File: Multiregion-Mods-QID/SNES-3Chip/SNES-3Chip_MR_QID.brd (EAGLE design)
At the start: 88.9 x 37.1 mm, 27 parts, among them IC1 74HC27D, IC2 74HC30D

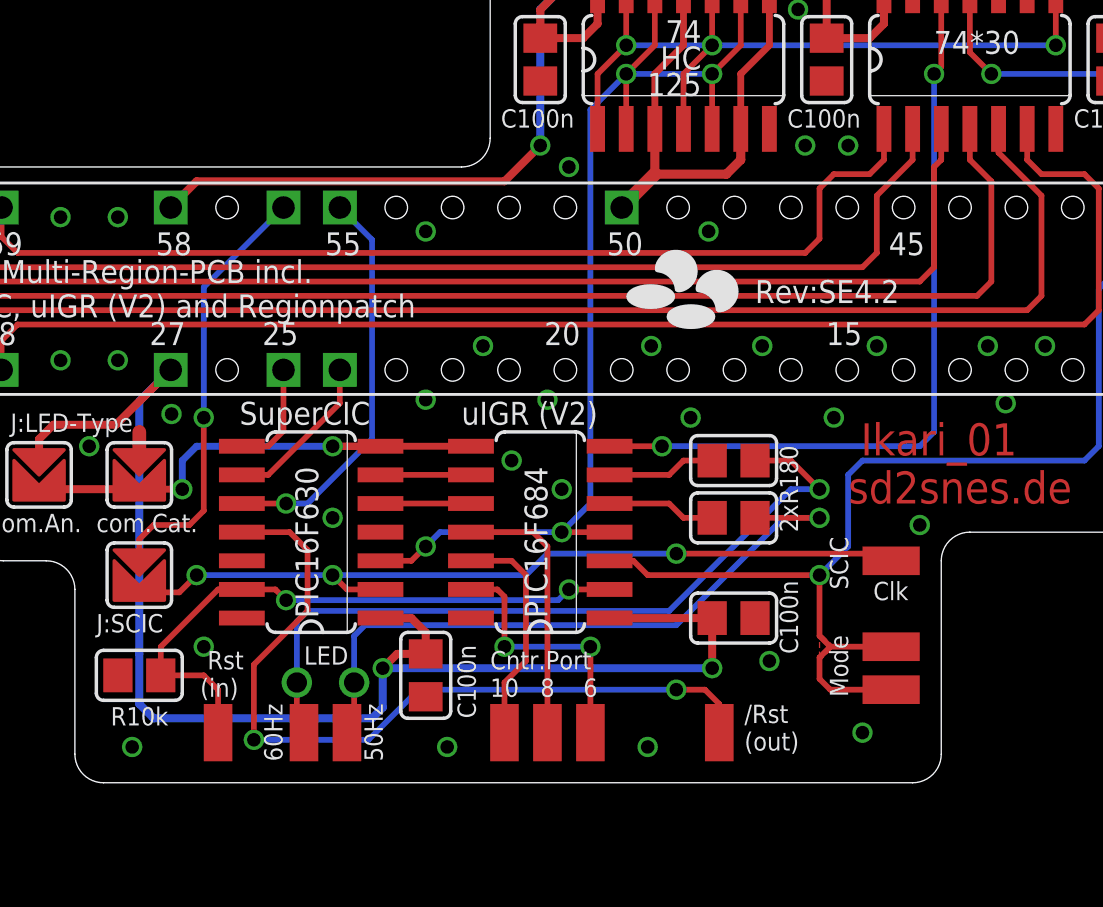
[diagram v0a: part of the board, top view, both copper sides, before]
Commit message: Minor Updates: - Dual design for crystals (SNES-1Chip_MR_QID only); SMD and THT crystals are now supported (If THT crystals are used, SMD pads have to isolated, manually.) - minor tweaks of traces - EAGLE Version 7.5.0
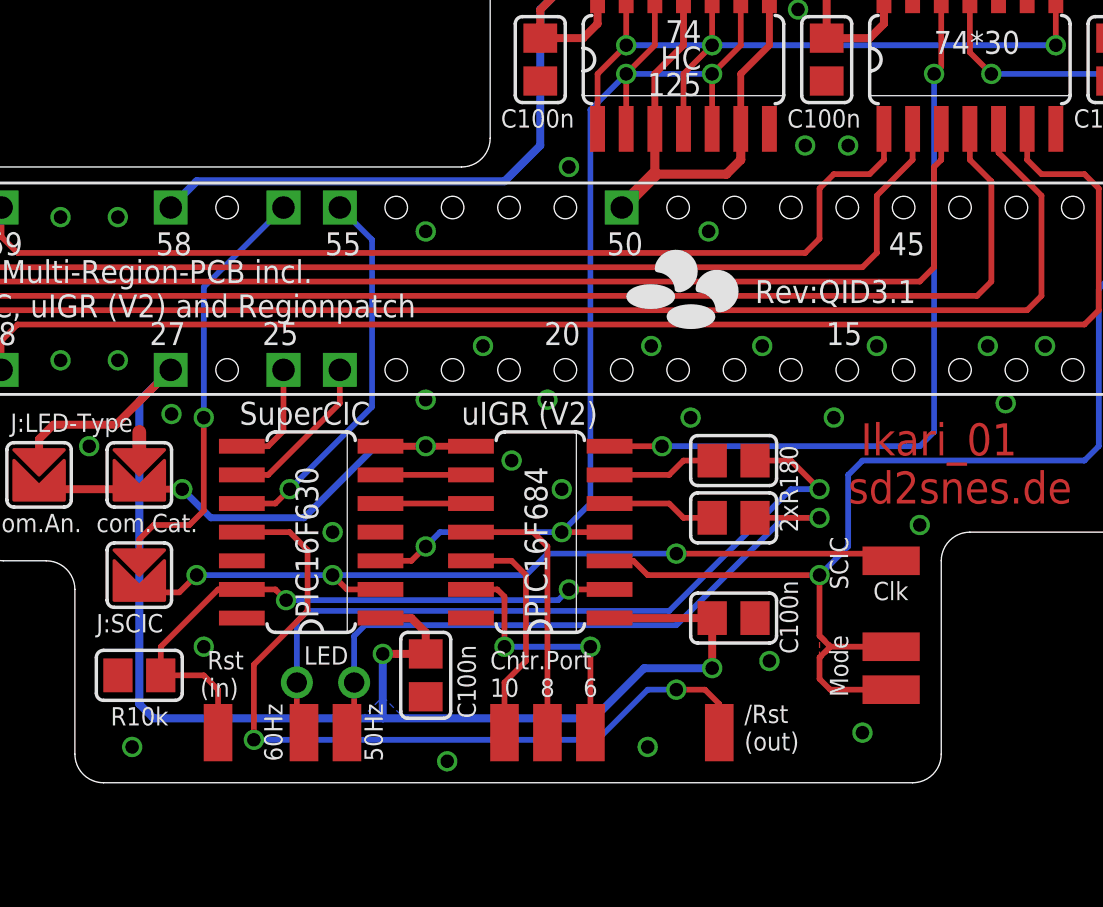
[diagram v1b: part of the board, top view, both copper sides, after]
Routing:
- net VCC: track 63.2 -> 64.8 mm
- net N$48: track 17.8 -> 17.0 mm
- net VCC_2: vias 4 -> 3
- added copper zone on layer 16, net VCC
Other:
- board text added: "Rev:QID3.1"
- board text removed: "Rev:SE4.2"
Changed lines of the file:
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@@
 <?xml version="1.0" encoding="utf-8"?>
 <!DOCTYPE eagle SYSTEM "eagle.dtd">
-<eagle version="7.4.0">
+<eagle version="7.5.0">
 <drawing>
 <settings>
@@
 <wire x1="52.3875" y1="15.875" x2="52.3875" y2="7.3025" width="0" layer="20"/>
 <wire x1="52.3875" y1="7.3025" x2="51.1175" y2="6.0325" width="0" layer="20" curve="-90"/>
-<text x="44.1325" y="27.305" size="1.016" layer="25" font="vector" ratio="12">Rev:SE4.2</text>
+<text x="44.1325" y="27.305" size="1.016" layer="25" font="vector" ratio="12">Rev:QID3.1</text>
 <polygon width="0.1" layer="21">
 <vertex x="40.534165625" y="27.590709375"/>
@@
 <signal name="GND">
 <contactref element="C1" pad="2"/>
-<via x="25.4" y="17.78" extent="1-16" drill="0.6"/>
+<via x="25.4" y="17.145" extent="1-16" drill="0.6"/>
 <via x="84.455" y="27.94" extent="1-16" drill="0.6"/>
 <via x="88.265" y="27.94" extent="1-16" drill="0.6"/>
@@
 <via x="44.45" y="25.4" extent="1-16" drill="0.6"/>
 <via x="19.685" y="12.065" extent="1-16" drill="0.6"/>
-<via x="30.48" y="7.62" extent="1-16" drill="0.6"/>
+<via x="30.48" y="6.985" extent="1-16" drill="0.6"/>
 <via x="33.655" y="41.275" extent="1-16" drill="0.6"/>
 <via x="39.52875" y="25.4" extent="1-16" drill="0.6"/>
@@
 <contactref element="C2" pad="1"/>
 <wire x1="37.6809" y1="13.335" x2="42.23" y2="13.335" width="0.3556" layer="1"/>
-<via x="27.6225" y="11.1125" extent="1-16" drill="0.6"/>
+<via x="27.6225" y="11.7475" extent="1-16" drill="0.6"/>
 <wire x1="27.5209" y1="13.335" x2="28.8925" y2="13.335" width="0.3556" layer="1"/>
 <wire x1="28.8925" y1="13.335" x2="29.5275" y2="12.7" width="0.3556" layer="1"/>
 <wire x1="29.5275" y1="12.7" x2="29.5275" y2="11.745" width="0.3556" layer="1"/>
-<wire x1="27.6225" y1="11.1125" x2="28.26" y2="11.7475" width="0.3556" layer="1"/>
 <wire x1="28.26" y1="11.7475" x2="29.5275" y2="11.745" width="0.3556" layer="1"/>
 <via x="42.23" y="11.115" extent="1-16" drill="0.6"/>
 <contactref element="U$6" pad="27"/>
 <wire x1="12.3825" y1="20.32" x2="12.3825" y2="21.2725" width="0.3556" layer="1"/>
-<wire x1="16.8275" y1="11.7475" x2="16.8275" y2="22.9475" width="0.3556" layer="16"/>
+<wire x1="16.8275" y1="9.525" x2="16.8275" y2="22.9475" width="0.3556" layer="16"/>
 <wire x1="16.8275" y1="22.9475" x2="18.22" y2="24.34" width="0.3556" layer="16"/>
 <wire x1="12.3825" y1="21.2725" x2="13.0175" y2="21.9075" width="0.3556" layer="1"/>
@@
 <wire x1="15.7875" y1="21.9075" x2="18.22" y2="24.34" width="0.3556" layer="1"/>
 <wire x1="42.23" y1="11.115" x2="42.23" y2="13.335" width="0.3556" layer="1"/>
-<wire x1="27.6225" y1="11.1125" x2="42.2275" y2="11.1125" width="0.3556" layer="16"/>
 <wire x1="42.2275" y1="11.1125" x2="42.23" y2="11.115" width="0.3048" layer="16"/>
-<wire x1="16.8275" y1="11.7475" x2="16.8275" y2="9.525" width="0.3556" layer="16"/>
 <wire x1="16.8275" y1="9.525" x2="17.4625" y2="8.89" width="0.3556" layer="16"/>
-<wire x1="17.4625" y1="8.89" x2="27.14625" y2="8.89" width="0.3556" layer="16"/>
-<wire x1="27.14625" y1="8.89" x2="27.6225" y2="9.36625" width="0.3556" layer="16"/>
-<wire x1="27.6225" y1="9.36625" x2="27.6225" y2="11.1125" width="0.3556" layer="16"/>
+<wire x1="17.4625" y1="8.89" x2="27.6225" y2="8.89" width="0.3556" layer="16"/>
+<wire x1="27.6225" y1="8.89" x2="36.98875" y2="8.89" width="0.3556" layer="16"/>
+<wire x1="42.2275" y1="11.1125" x2="39.21125" y2="11.1125" width="0.3556" layer="16"/>
+<wire x1="39.21125" y1="11.1125" x2="36.98875" y2="8.89" width="0.3556" layer="16"/>
+<wire x1="27.6225" y1="11.7475" x2="27.6225" y2="8.89" width="0.3556" layer="16"/>
+<wire x1="28.26" y1="11.7475" x2="27.6225" y2="11.7475" width="0.3556" layer="1"/>
+<polygon width="0.3556" layer="16">
+<vertex x="26.67" y="8.89"/>
+<vertex x="27.6225" y="9.8425"/>
+<vertex x="28.575" y="8.89"/>
+</polygon>
 </signal>
 <signal name="N$42">
@@
 <contactref element="IC2" pad="14"/>
 <contactref element="74HC(T)125" pad="14"/>
-<wire x1="18.22" y1="31.54" x2="18.22" y2="31.555" width="0.3048" layer="1"/>
-<wire x1="18.22" y1="31.555" x2="19.3675" y2="32.7025" width="0.3556" layer="1"/>
-<via x="34.6075" y="34.29" extent="1-16" drill="0.6"/>
 <wire x1="35.56" y1="41.275" x2="47.3075" y2="41.275" width="0.3556" layer="16"/>
 <via x="60.0075" y="41.275" extent="1-16" drill="0.6"/>
@@
 <wire x1="47.31" y1="39.0525" x2="47.3075" y2="39.0525" width="0.3048" layer="1"/>
 <wire x1="47.3075" y1="39.0525" x2="47.3075" y2="41.275" width="0.3556" layer="1"/>
-<wire x1="19.3675" y1="32.7025" x2="33.02" y2="32.7025" width="0.3556" layer="1"/>
-<wire x1="33.02" y1="32.7025" x2="34.6075" y2="34.29" width="0.3556" layer="1"/>
 <wire x1="35.56" y1="41.275" x2="34.6075" y2="40.3225" width="0.3556" layer="16"/>
 <wire x1="34.6075" y1="40.3225" x2="34.6075" y2="34.29" width="0.3556" layer="16"/>
+<wire x1="18.22" y1="31.555" x2="19.3675" y2="32.7025" width="0.3556" layer="16"/>
+<wire x1="19.3675" y1="32.7025" x2="33.02" y2="32.7025" width="0.3556" layer="16"/>
+<wire x1="33.02" y1="32.7025" x2="34.6075" y2="34.29" width="0.3556" layer="16"/>
+<wire x1="18.22" y1="31.555" x2="18.22" y2="31.54" width="0" layer="19" extent="16-16"/>
 </signal>
 <signal name="N$39">
@@
 <contactref element="U$2" pad="10"/>
 <contactref element="U$6" pad="55"/>
-<wire x1="27.14625" y1="21.2725" x2="27.14625" y2="30.11375" width="0.254" layer="16"/>
 <wire x1="27.14625" y1="30.11375" x2="25.72" y2="31.54" width="0.254" layer="16"/>
-<wire x1="21.3741" y1="18.415" x2="23.33625" y2="18.415" width="0.254" layer="1"/>
-<via x="23.33625" y="18.415" extent="1-16" drill="0.6"/>
-<wire x1="23.33625" y1="18.415" x2="24.28875" y2="18.415" width="0.254" layer="16"/>
-<wire x1="24.28875" y1="18.415" x2="27.14625" y2="21.2725" width="0.254" layer="16"/>
+<via x="23.495" y="19.05" extent="1-16" drill="0.6"/>
+<wire x1="21.3741" y1="18.415" x2="22.86" y2="18.415" width="0.254" layer="1"/>
+<wire x1="22.86" y1="18.415" x2="23.495" y2="19.05" width="0.254" layer="1"/>
+<wire x1="27.14625" y1="30.11375" x2="27.14625" y2="22.70125" width="0.254" layer="16"/>
+<wire x1="27.14625" y1="22.70125" x2="23.495" y2="19.05" width="0.254" layer="16"/>
 </signal>
 <signal name="N$49">
@@
 <wire x1="41.91" y1="10.16" x2="42.545" y2="9.525" width="0.254" layer="1"/>
 <wire x1="42.545" y1="9.525" x2="42.545" y2="8.255" width="0.254" layer="1"/>
-<wire x1="21.9075" y1="7.9375" x2="26.9875" y2="7.9375" width="0.254" layer="16"/>
-<wire x1="26.9875" y1="7.9375" x2="29.21" y2="10.16" width="0.254" layer="16"/>
-<wire x1="29.21" y1="10.16" x2="40.64" y2="10.16" width="0.254" layer="16"/>
+<wire x1="21.9075" y1="7.9375" x2="37.1475" y2="7.9375" width="0.254" layer="16"/>
+<wire x1="37.1475" y1="7.9375" x2="39.37" y2="10.16" width="0.254" layer="16"/>
+<wire x1="39.37" y1="10.16" x2="40.64" y2="10.16" width="0.254" layer="16"/>
 </signal>
 <signal name="N$10">
@@
 <contactref element="U$2" pad="7"/>
 <contactref element="U$4" pad="P$2"/>
-<wire x1="27.5209" y1="20.955" x2="25.4" y2="20.955" width="0.3048" layer="1"/>
-<wire x1="25.4" y1="20.955" x2="31.5341" y2="20.955" width="0.3048" layer="1"/>
-<via x="25.4" y="20.955" extent="1-16" drill="0.6"/>
+<wire x1="27.5209" y1="20.955" x2="29.5275" y2="20.955" width="0.3048" layer="1"/>
+<wire x1="29.5275" y1="20.955" x2="31.5341" y2="20.955" width="0.3048" layer="1"/>
+<via x="29.5275" y="20.955" extent="1-16" drill="0.6"/>
 <contactref element="U$5" pad="P$2"/>
-<wire x1="19.3675" y1="20.955" x2="25.4" y2="20.955" width="0.3048" layer="16"/>
-<wire x1="19.3675" y1="20.955" x2="18.7325" y2="20.32" width="0.3048" layer="16"/>
 <wire x1="16.8275" y1="18.919825" x2="17.014825" y2="18.919825" width="0.3048" layer="1"/>
 <wire x1="17.014825" y1="18.919825" x2="17.145" y2="19.05" width="0.3048" layer="1"/>
 <wire x1="17.145" y1="19.05" x2="18.7325" y2="19.05" width="0.3048" layer="1"/>
 <via x="18.7325" y="19.05" extent="1-16" drill="0.6"/>
-<wire x1="18.7325" y1="19.05" x2="18.7325" y2="20.32" width="0.3048" layer="16"/>
 <wire x1="12.3825" y1="18.919825" x2="12.569825" y2="18.919825" width="0.3048" layer="1"/>
 <wire x1="12.569825" y1="18.919825" x2="12.7" y2="19.05" width="0.3048" layer="1"/>
 <wire x1="12.7" y1="19.05" x2="16.697325" y2="19.05" width="0.3556" layer="1"/>
 <wire x1="16.697325" y1="19.05" x2="16.8275" y2="18.919825" width="0.3048" layer="1"/>
+<wire x1="18.7325" y1="19.05" x2="20.0025" y2="17.78" width="0.3048" layer="16"/>
+<wire x1="20.0025" y1="17.78" x2="24.13" y2="17.78" width="0.3048" layer="16"/>
+<wire x1="29.5275" y1="20.955" x2="27.305" y2="20.955" width="0.3048" layer="16"/>
+<wire x1="27.305" y1="20.955" x2="24.13" y2="17.78" width="0.3048" layer="16"/>
 </signal>
 <signal name="N$33">
@@
 <wire x1="45.4025" y1="17.78" x2="40.64" y2="13.0175" width="0.254" layer="16"/>
 <wire x1="40.64" y1="13.0175" x2="26.82875" y2="13.0175" width="0.254" layer="16"/>
-<via x="26.3525" y="10.4775" extent="1-16" drill="0.9"/>
+<via x="26.3525" y="10.4775" extent="1-16" drill="0.9" diameter="1.4224" alwaysstop="yes"/>
 <wire x1="26.3525" y1="10.4775" x2="26.3525" y2="8.5725" width="0.254" layer="1"/>
 <wire x1="26.3525" y1="8.5725" x2="26.035" y2="8.255" width="0.254" layer="1"/>
@@
 <wire x1="45.72" y1="19.05" x2="40.3225" y2="13.6525" width="0.254" layer="16"/>
 <wire x1="40.3225" y1="13.6525" x2="24.28875" y2="13.6525" width="0.254" layer="16"/>
-<via x="23.8125" y="10.4775" extent="1-16" drill="0.9"/>
+<via x="23.8125" y="10.4775" extent="1-16" drill="0.9" diameter="1.4224" alwaysstop="yes"/>
 <wire x1="23.8125" y1="10.4775" x2="23.8125" y2="8.5725" width="0.254" layer="1"/>
 <wire x1="23.8125" y1="8.5725" x2="24.13" y2="8.255" width="0.254" layer="1"/>

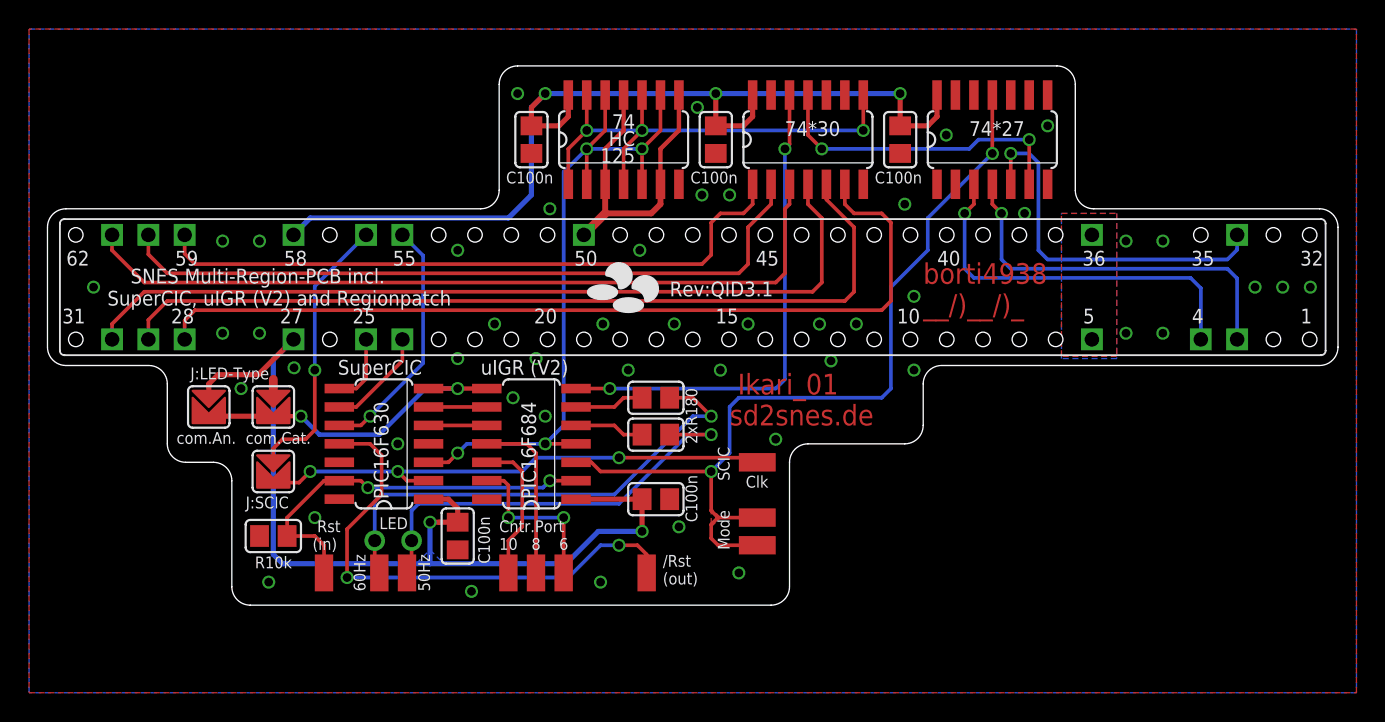
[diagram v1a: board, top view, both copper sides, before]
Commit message: add thermals to ground pad (easier to solder) and reduce PCB size a bit
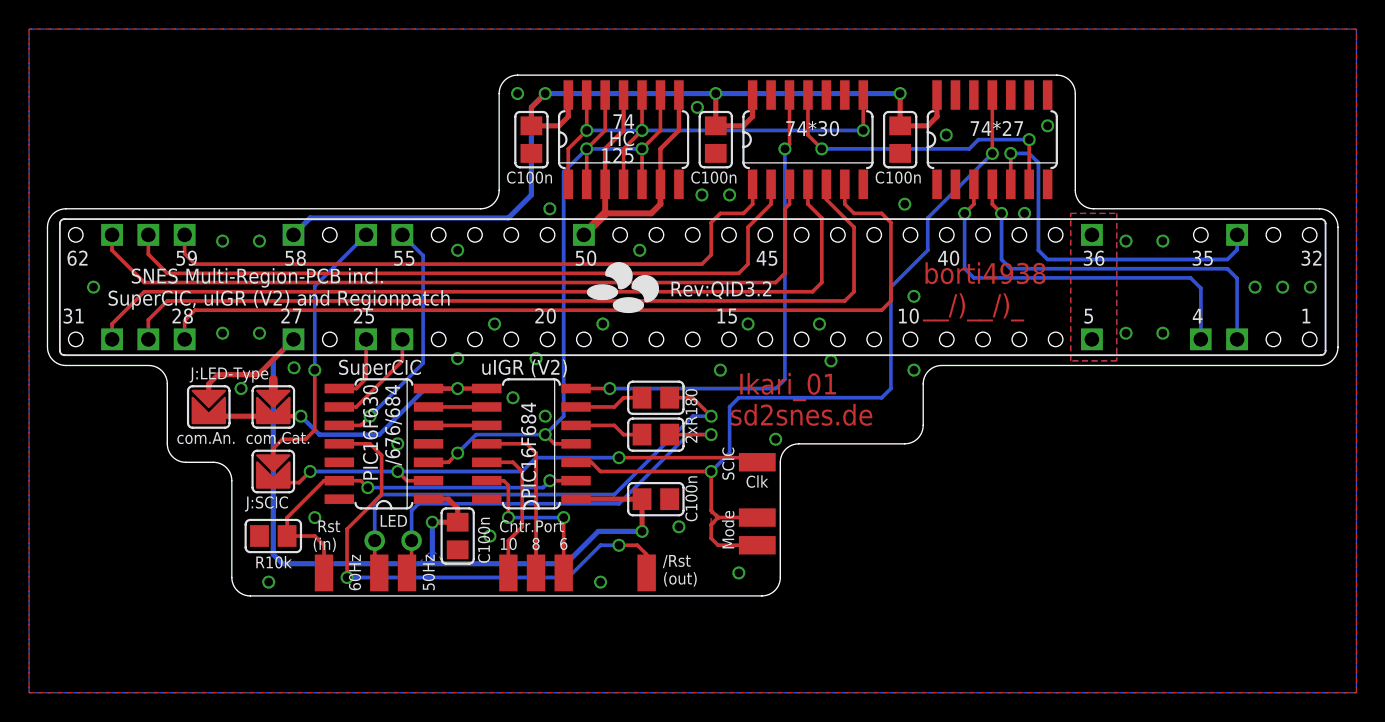
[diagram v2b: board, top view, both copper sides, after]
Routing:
- net GND: vias 48 -> 45
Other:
- board size 88.9 x 37.1 mm -> 88.9 x 35.9 mm
- board text added: "PIC16F630 /676/684"
- board text added: "Rev:QID3.2"
- board text removed: "PIC16F630"
- board text removed: "Rev:QID3.1"
